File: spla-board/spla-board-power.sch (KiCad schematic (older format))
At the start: 68 parts, among them J12 J_POWER, J7 Barrel_Jack, SW2 SW_DPDT_x2, U14 TLV73311PDBV, U7 ST1S10PHR, U8 ST1S10PHR, U9 TLV73325PDBV

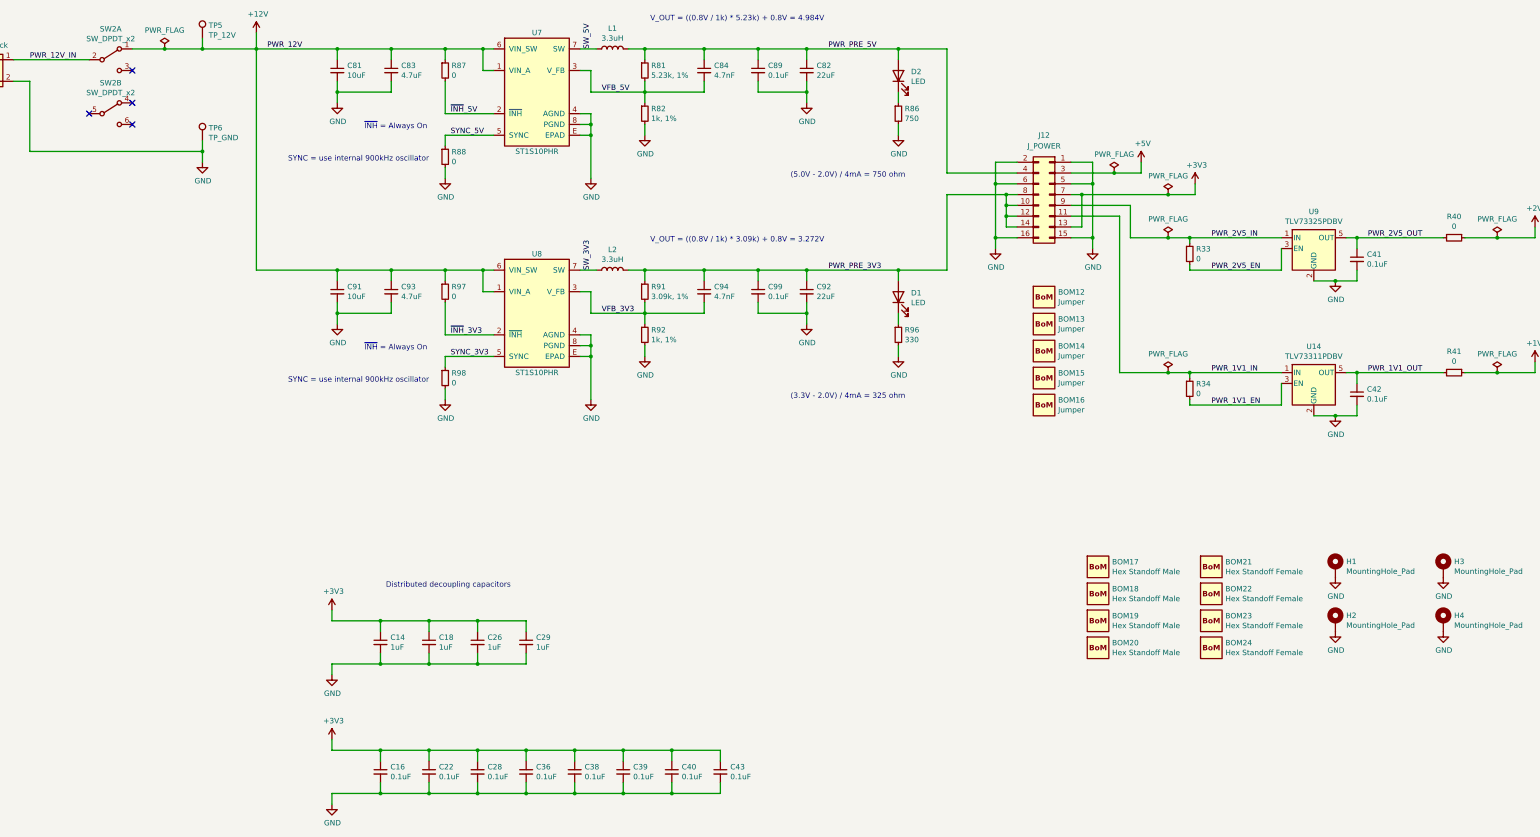
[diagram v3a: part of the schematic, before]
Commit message: schematic/pcb: Remove unnecessary 0-ohm resistors; renumber all parts by value.
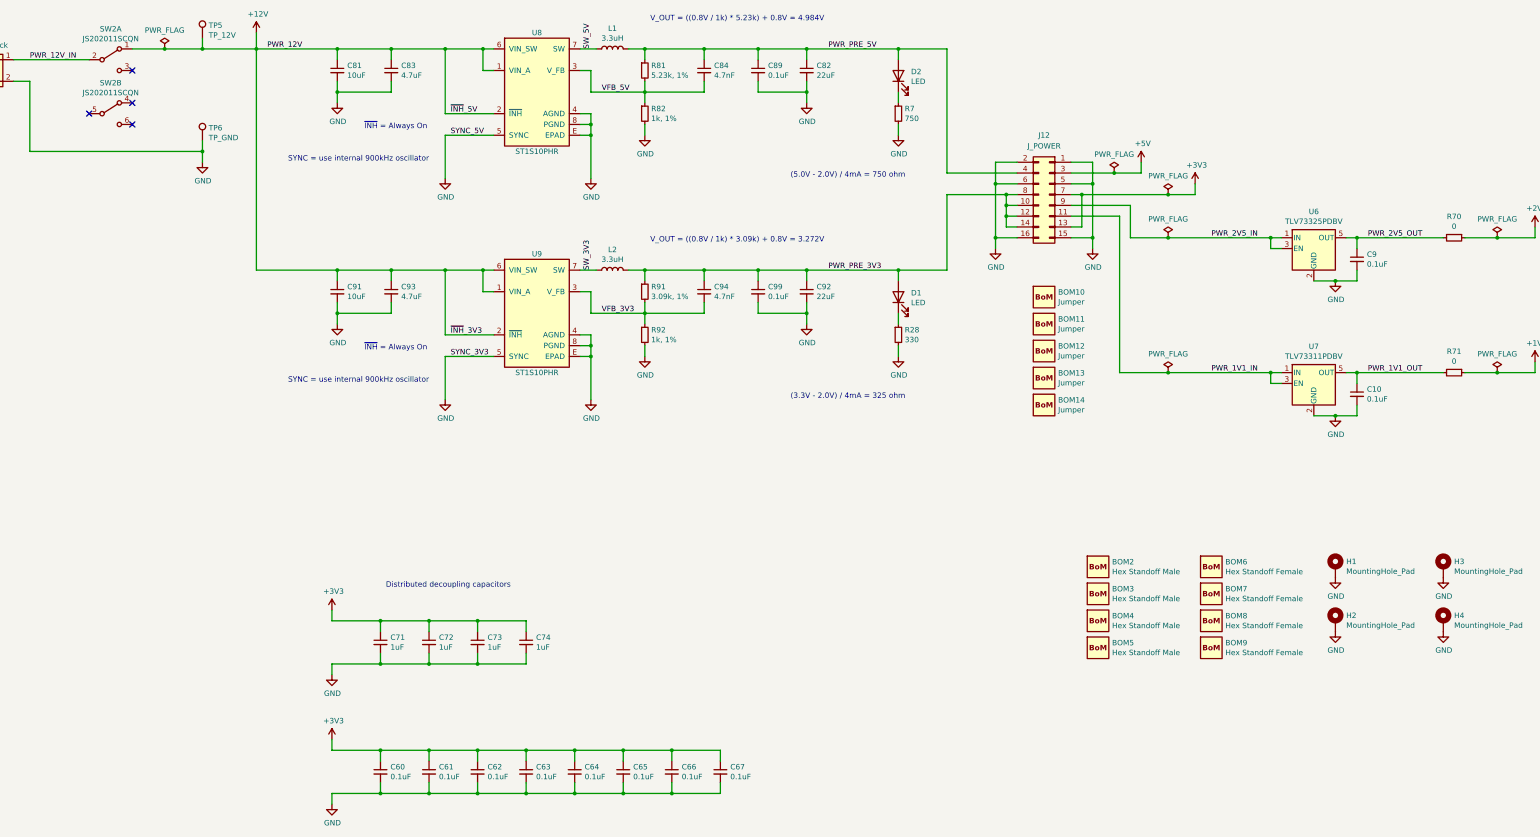
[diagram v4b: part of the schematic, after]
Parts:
- removed R33, R34, R87, R88, R97, R98: 0, Resistor_SMD:R_0603_1608Metric, symbol Device:R_Small
- SW2: value SW_DPDT_x2 -> JS202011SCQN
- renumbered BOM12 to BOM10, BOM13 to BOM11, BOM14 to BOM12, BOM15 to BOM13, BOM16 to BOM14, BOM17 to BOM2, BOM18 to BOM3, BOM19 to BOM4, BOM20 to BOM5, BOM21 to BOM6, BOM22 to BOM7, BOM23 to BOM8, BOM24 to BOM9, C42 to C10, C16 to C60, C22 to C61, C28 to C62, C36 to C63, C38 to C64, C39 to C65, C40 to C66, C43 to C67, C14 to C71, C18 to C72, C26 to C73, C29 to C74, C41 to C9, R96 to R28, R86 to R7, R40 to R70, R41 to R71, U9 to U6, U14 to U7, U7 to U8, U8 to U9
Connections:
- net PWR_1V1_EN is gone; now on net PWR_1V1_IN: U7.3 (EN)
- net PWR_2V5_EN is gone; now on net PWR_2V5_IN: U6.3 (EN)
- net SYNC_3V3 is gone; now on net GND: U9.5 (SYNC)
- net SYNC_5V is gone; now on net GND: U8.5 (SYNC)
- net ~INH~_3V3 is gone; now on net +12V: U9.2 (~INH)
- net ~INH~_5V is gone; now on net +12V: U8.2 (~INH)

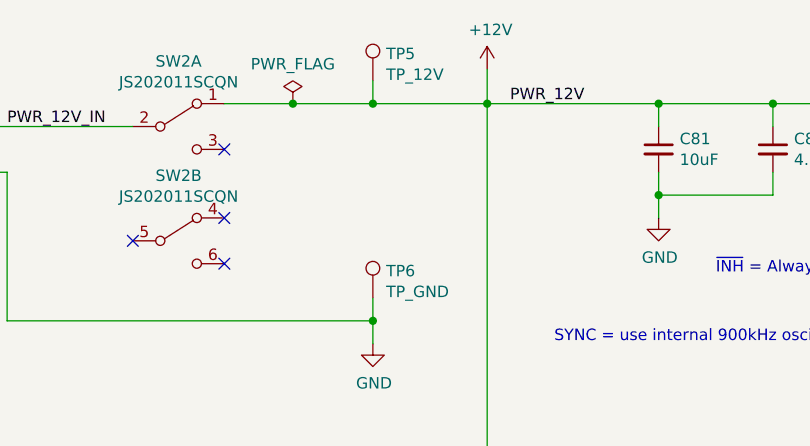
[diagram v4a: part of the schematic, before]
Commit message: schematic/pcb: Add 12mhz clock test point; renumber test points.
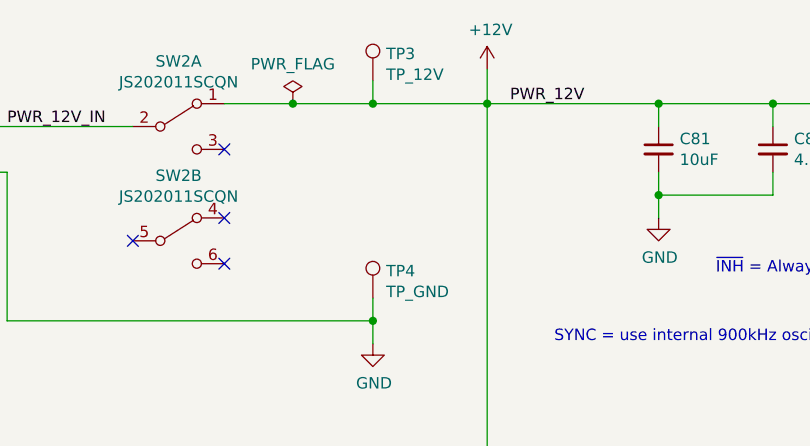
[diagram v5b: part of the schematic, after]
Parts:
- renumbered TP5 to TP3, TP6 to TP4
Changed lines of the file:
@@
 	11600 4500 11350 4500
 $Comp
-L Connector:TestPoint TP5
+L Connector:TestPoint TP3
 U 1 1 5E6077CA
 P 2900 3250
-F 0 "TP5" H 2958 3368 50  0000 L CNN
+F 0 "TP3" H 2958 3368 50  0000 L CNN
 F 1 "TP_12V" H 2958 3277 50  0000 L CNN
 F 2 "TestPoint:TestPoint_Pad_D2.0mm" H 3100 3250 50  0001 C CNN
@@
 	4100 10250 4100 10350
 $Comp
-L Connector:TestPoint TP6
+L Connector:TestPoint TP4
 U 1 1 5EAFCBB1
 P 2900 4200
-F 0 "TP6" H 2958 4318 50  0000 L CNN
+F 0 "TP4" H 2958 4318 50  0000 L CNN
 F 1 "TP_GND" H 2958 4227 50  0000 L CNN
 F 2 "TestPoint:TestPoint_Pad_D2.0mm" H 3100 4200 50  0001 C CNN

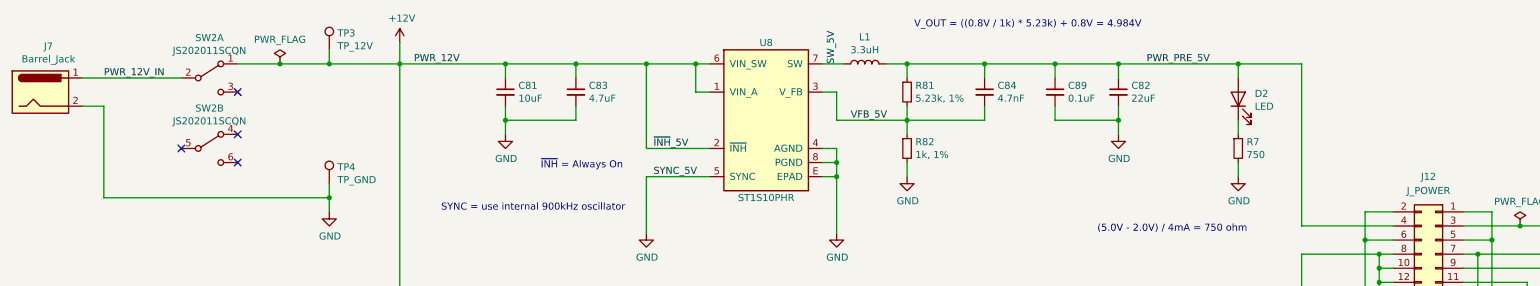
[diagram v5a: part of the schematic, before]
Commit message: schematic/pcb: Renumber connectors (J*).
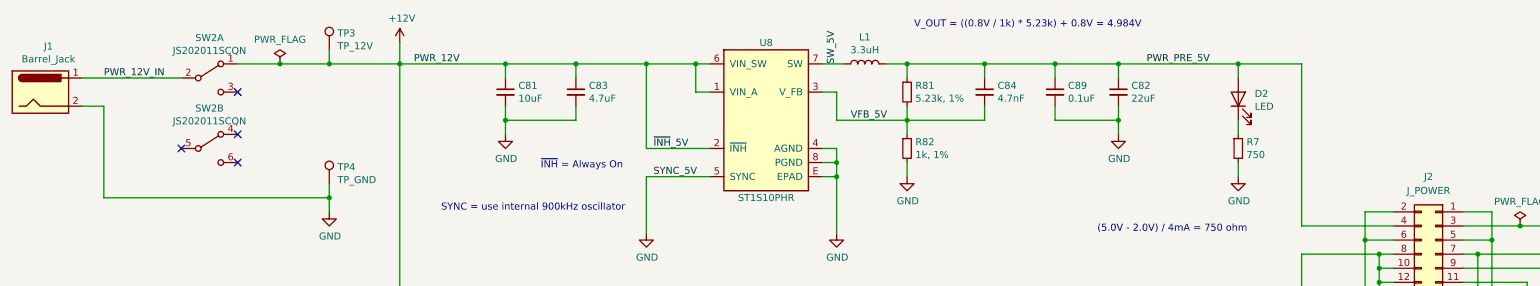
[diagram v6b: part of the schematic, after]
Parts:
- renumbered J7 to J1, J12 to J2
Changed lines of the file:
@@
 $EndDescr
 $Comp
-L Connector:Barrel_Jack J7
+L Connector:Barrel_Jack J1
 U 1 1 5E532515
 P 850 3550
-F 0 "J7" H 907 3875 50  0000 C CNN
+F 0 "J1" H 907 3875 50  0000 C CNN
 F 1 "Barrel_Jack" H 907 3784 50  0000 C CNN
 F 2 "Connector_BarrelJack:BarrelJack_CUI_PJ-036AH-SMT_Horizontal" H 900 3510 50  0001 C CNN
@@
 Connection ~ 10350 4900
 $Comp
-L Connector_Generic:Conn_02x08_Odd_Even J12
+L Connector_Generic:Conn_02x08_Odd_Even J2
 U 1 1 5E5D4B8F
 P 10750 4700
-F 0 "J12" H 10800 5250 50  0000 C CNN
+F 0 "J2" H 10800 5250 50  0000 C CNN
 F 1 "J_POWER" H 10800 5150 50  0000 C CNN
 F 2 "Connector_PinHeader_2.54mm:PinHeader_2x08_P2.54mm_Vertical" H 10750 4700 50  0001 C CNN

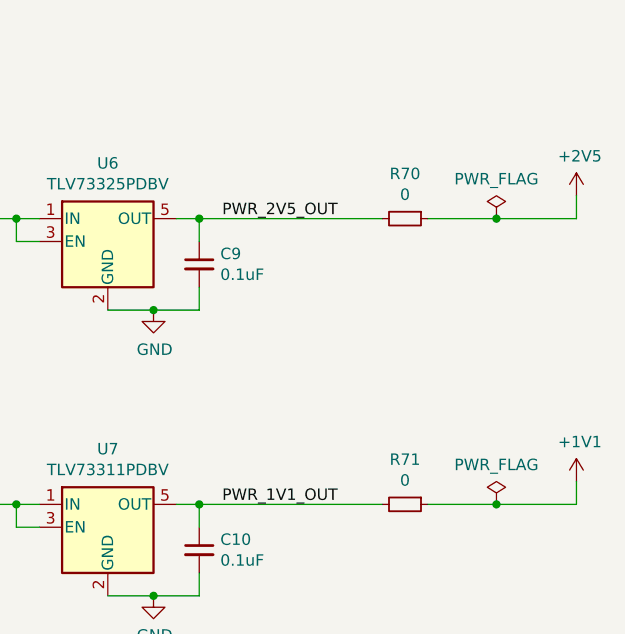
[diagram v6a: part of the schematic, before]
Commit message: schematic/pcb: Seperate PPU2 AVCC; add more PPU decoupling.
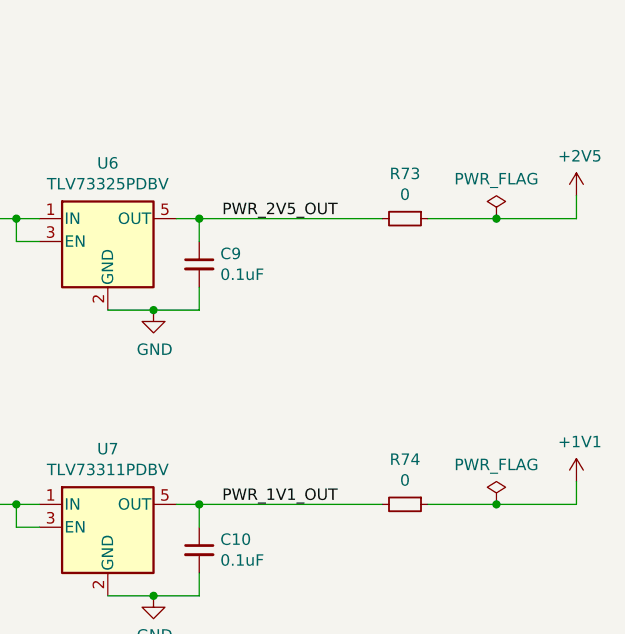
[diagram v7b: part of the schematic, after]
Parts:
- renumbered R70 to R73, R71 to R74
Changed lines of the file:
@@
 	3400 3200 3400 3350
 $Comp
-L Device:R_Small R70
+L Device:R_Small R73
 U 1 1 5FB785AC
 P 14500 5100
-F 0 "R70" V 14304 5100 50  0000 C CNN
+F 0 "R73" V 14304 5100 50  0000 C CNN
 F 1 "0" V 14395 5100 50  0000 C CNN
 F 2 "Resistor_SMD:R_0603_1608Metric" H 14500 5100 50  0001 C CNN
@@
 $EndComp
 $Comp
-L Device:R_Small R71
+L Device:R_Small R74
 U 1 1 5FB7903C
 P 14500 6350
-F 0 "R71" V 14304 6350 50  0000 C CNN
+F 0 "R74" V 14304 6350 50  0000 C CNN
 F 1 "0" V 14395 6350 50  0000 C CNN
 F 2 "Resistor_SMD:R_0603_1608Metric" H 14500 6350 50  0001 C CNN

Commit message: schematic: Swap hex standoffs for shorter ones (3.5cm to 2.0cm).
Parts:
- BOM2, BOM3, BOM4, BOM5: Digikey 732-12823-ND -> 732-12817-ND; Manufacturer Id 971350366 -> 971200366
- BOM6, BOM7, BOM8, BOM9: Digikey 732-12808-ND -> 732-12802-ND; Manufacturer Id 970350366 -> 970200366
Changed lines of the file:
@@
 F 2 "SPLA:BoM" H 11200 8150 50  0001 C CNN
 F 3 "" H 11200 8150 50  0001 C CNN
-F 4 "732-12823-ND" H 11200 8150 50  0001 C CNN "Digikey"
-F 5 "971350366" H 11200 8150 50  0001 C CNN "Manufacturer Id"
+F 4 "732-12817-ND" H 11200 8150 50  0001 C CNN "Digikey"
+F 5 "971200366" H 11200 8150 50  0001 C CNN "Manufacturer Id"
 F 6 "Wuerth Electronik" H 11200 8150 50  0001 C CNN "Manufacturer"
 	1    11200 8150
@@
 F 2 "SPLA:BoM" H 11200 8400 50  0001 C CNN
 F 3 "" H 11200 8400 50  0001 C CNN
-F 4 "732-12823-ND" H 11200 8400 50  0001 C CNN "Digikey"
-F 5 "971350366" H 11200 8400 50  0001 C CNN "Manufacturer Id"
+F 4 "732-12817-ND" H 11200 8400 50  0001 C CNN "Digikey"
+F 5 "971200366" H 11200 8400 50  0001 C CNN "Manufacturer Id"
 F 6 "Wuerth Electronik" H 11200 8400 50  0001 C CNN "Manufacturer"
 	1    11200 8400
@@
 F 2 "SPLA:BoM" H 11200 8650 50  0001 C CNN
 F 3 "" H 11200 8650 50  0001 C CNN
-F 4 "732-12823-ND" H 11200 8650 50  0001 C CNN "Digikey"
-F 5 "971350366" H 11200 8650 50  0001 C CNN "Manufacturer Id"
+F 4 "732-12817-ND" H 11200 8650 50  0001 C CNN "Digikey"
+F 5 "971200366" H 11200 8650 50  0001 C CNN "Manufacturer Id"
 F 6 "Wuerth Electronik" H 11200 8650 50  0001 C CNN "Manufacturer"
 	1    11200 8650
@@
 F 2 "SPLA:BoM" H 11200 8900 50  0001 C CNN
 F 3 "" H 11200 8900 50  0001 C CNN
-F 4 "732-12823-ND" H 11200 8900 50  0001 C CNN "Digikey"
-F 5 "971350366" H 11200 8900 50  0001 C CNN "Manufacturer Id"
+F 4 "732-12817-ND" H 11200 8900 50  0001 C CNN "Digikey"
+F 5 "971200366" H 11200 8900 50  0001 C CNN "Manufacturer Id"
 F 6 "Wuerth Electronik" H 11200 8900 50  0001 C CNN "Manufacturer"
 	1    11200 8900
@@
 F 2 "SPLA:BoM" H 12250 8150 50  0001 C CNN
 F 3 "" H 12250 8150 50  0001 C CNN
-F 4 "732-12808-ND" H 12250 8150 50  0001 C CNN "Digikey"
-F 5 "970350366" H 12250 8150 50  0001 C CNN "Manufacturer Id"
+F 4 "732-12802-ND" H 12250 8150 50  0001 C CNN "Digikey"
+F 5 "970200366" H 12250 8150 50  0001 C CNN "Manufacturer Id"
 F 6 "Wuerth Electronik" H 12250 8150 50  0001 C CNN "Manufacturer"
 	1    12250 8150
@@
 F 2 "SPLA:BoM" H 12250 8400 50  0001 C CNN
 F 3 "" H 12250 8400 50  0001 C CNN
-F 4 "732-12808-ND" H 12250 8400 50  0001 C CNN "Digikey"
-F 5 "970350366" H 12250 8400 50  0001 C CNN "Manufacturer Id"
+F 4 "732-12802-ND" H 12250 8400 50  0001 C CNN "Digikey"
+F 5 "970200366" H 12250 8400 50  0001 C CNN "Manufacturer Id"
 F 6 "Wuerth Electronik" H 12250 8400 50  0001 C CNN "Manufacturer"
 	1    12250 8400
@@
 F 2 "SPLA:BoM" H 12250 8650 50  0001 C CNN
 F 3 "" H 12250 8650 50  0001 C CNN
-F 4 "732-12808-ND" H 12250 8650 50  0001 C CNN "Digikey"
-F 5 "970350366" H 12250 8650 50  0001 C CNN "Manufacturer Id"
+F 4 "732-12802-ND" H 12250 8650 50  0001 C CNN "Digikey"
+F 5 "970200366" H 12250 8650 50  0001 C CNN "Manufacturer Id"
 F 6 "Wuerth Electronik" H 12250 8650 50  0001 C CNN "Manufacturer"
 	1    12250 8650
@@
 F 2 "SPLA:BoM" H 12250 8900 50  0001 C CNN
 F 3 "" H 12250 8900 50  0001 C CNN
-F 4 "732-12808-ND" H 12250 8900 50  0001 C CNN "Digikey"
-F 5 "970350366" H 12250 8900 50  0001 C CNN "Manufacturer Id"
+F 4 "732-12802-ND" H 12250 8900 50  0001 C CNN "Digikey"
+F 5 "970200366" H 12250 8900 50  0001 C CNN "Manufacturer Id"
 F 6 "Wuerth Electronik" H 12250 8900 50  0001 C CNN "Manufacturer"
 	1    12250 8900
